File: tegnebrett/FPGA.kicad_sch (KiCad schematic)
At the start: 28 parts, among them J6 FPGA_debug1, J7 FPGA_Header_Pin, SW6 FPGA_Button, U2 XC7A100T-2FTG256I, U3 Oscillator 100MHz, U4 IS66WVH16M8DBLL-100B1LI1

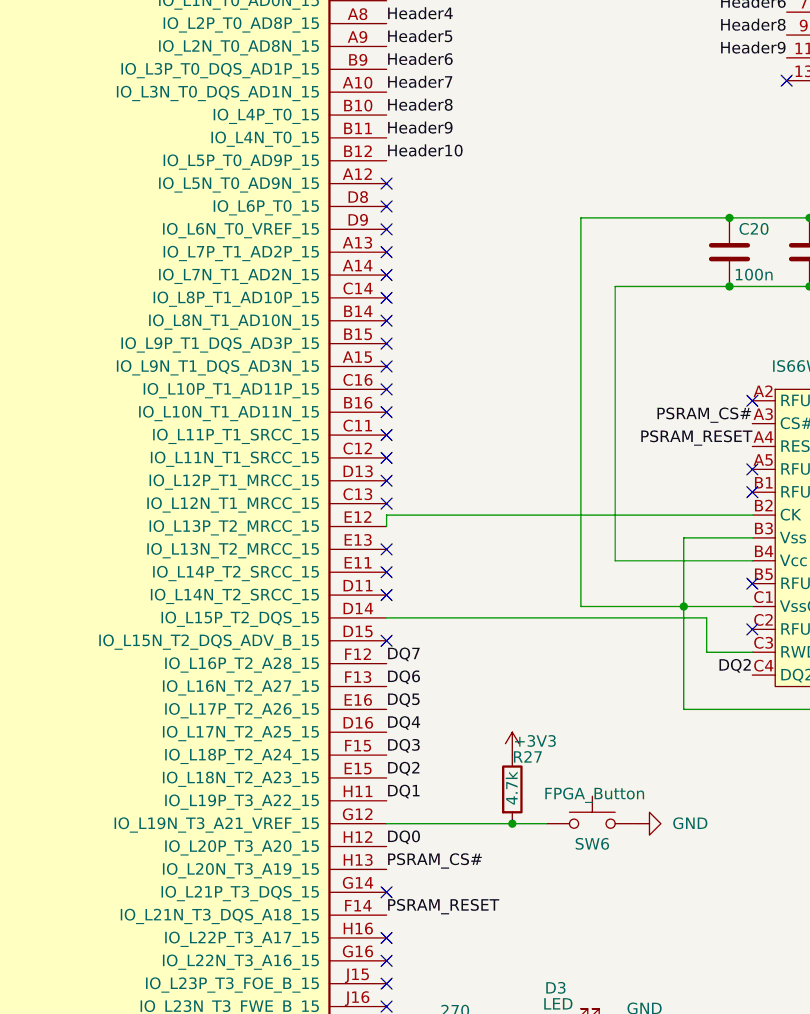
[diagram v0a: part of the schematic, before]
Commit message: refactor(FPGA): move DQ0 pin to reference to different GPIO pin
As Tormod wrote on Discord:
H12 (DQ0) -> A12 (IO_L5N_TO_AD9N_15)
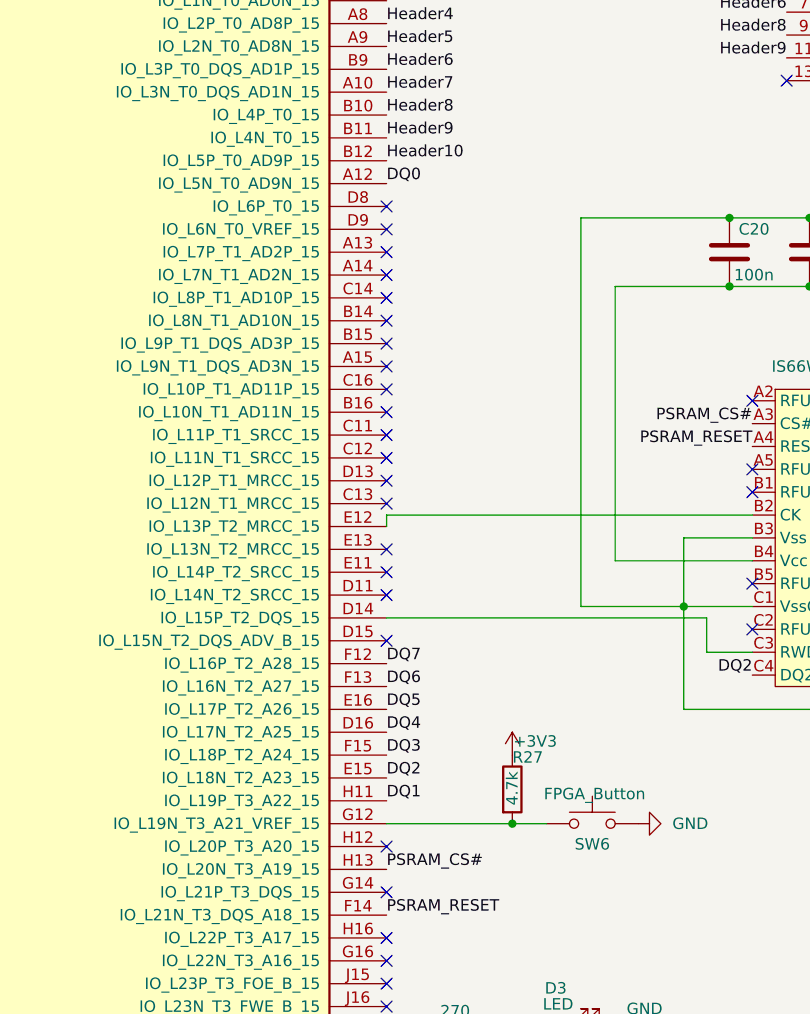
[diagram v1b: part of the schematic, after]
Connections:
- net DQ0: now also U2.A12 (IO_L5N_T0_AD9N_15); no longer U2.H12 (IO_L20P_T3_A20_15)
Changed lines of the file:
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@@
+	)
+	(no_connect
+		(at 320.04 147.32)
 	)
 	(no_connect
@@
 	(no_connect
 		(at 360.68 97.79)
-	)
-	(no_connect
-		(at 320.04 73.66)
 	)
 	(no_connect
@@
 		)
 	)
-	(label "DQ0"
-		(at 320.04 147.32 0)
-		(effects
-			(font
-				(size 1.27 1.27)
-			)
-			(justify left bottom)
-		)
-	)
 	(label "DQ5"
 		(at 391.16 119.38 0)
@@
 		(effects
 			(font
+				(size 1.27 1.27)
+			)
+			(justify left bottom)
+		)
+	)
+	(label "DQ0"
+		(at 320.04 73.66 0)
+		(effects
+			(font

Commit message: fix: add FPGA debug symbol to tegnebrett_symbols library
This was a symbol added by Tormod which has also been lost to time.
No problems, we just save the symbol into *tegnebrett_symbols*.

I believe we will change the pin functions as well.
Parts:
- J6: value FPGA_debug1 -> FPGA_debug; symbol GD25F128FS2GR:FPGA_debug -> tegnebrett_symbols:FPGA_debug
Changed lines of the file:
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@@
 	)
 	(symbol
-		(lib_id "GD25F128FS2GR:FPGA_debug")
+		(lib_id "tegnebrett_symbols:FPGA_debug")
 		(at 106.68 21.59 0)
 		(mirror y)
@@
 			)
 		)
-		(property "Value" "FPGA_debug1"
+		(property "Value" "FPGA_debug"
 			(at 107.95 20.32 0)
 			(effects

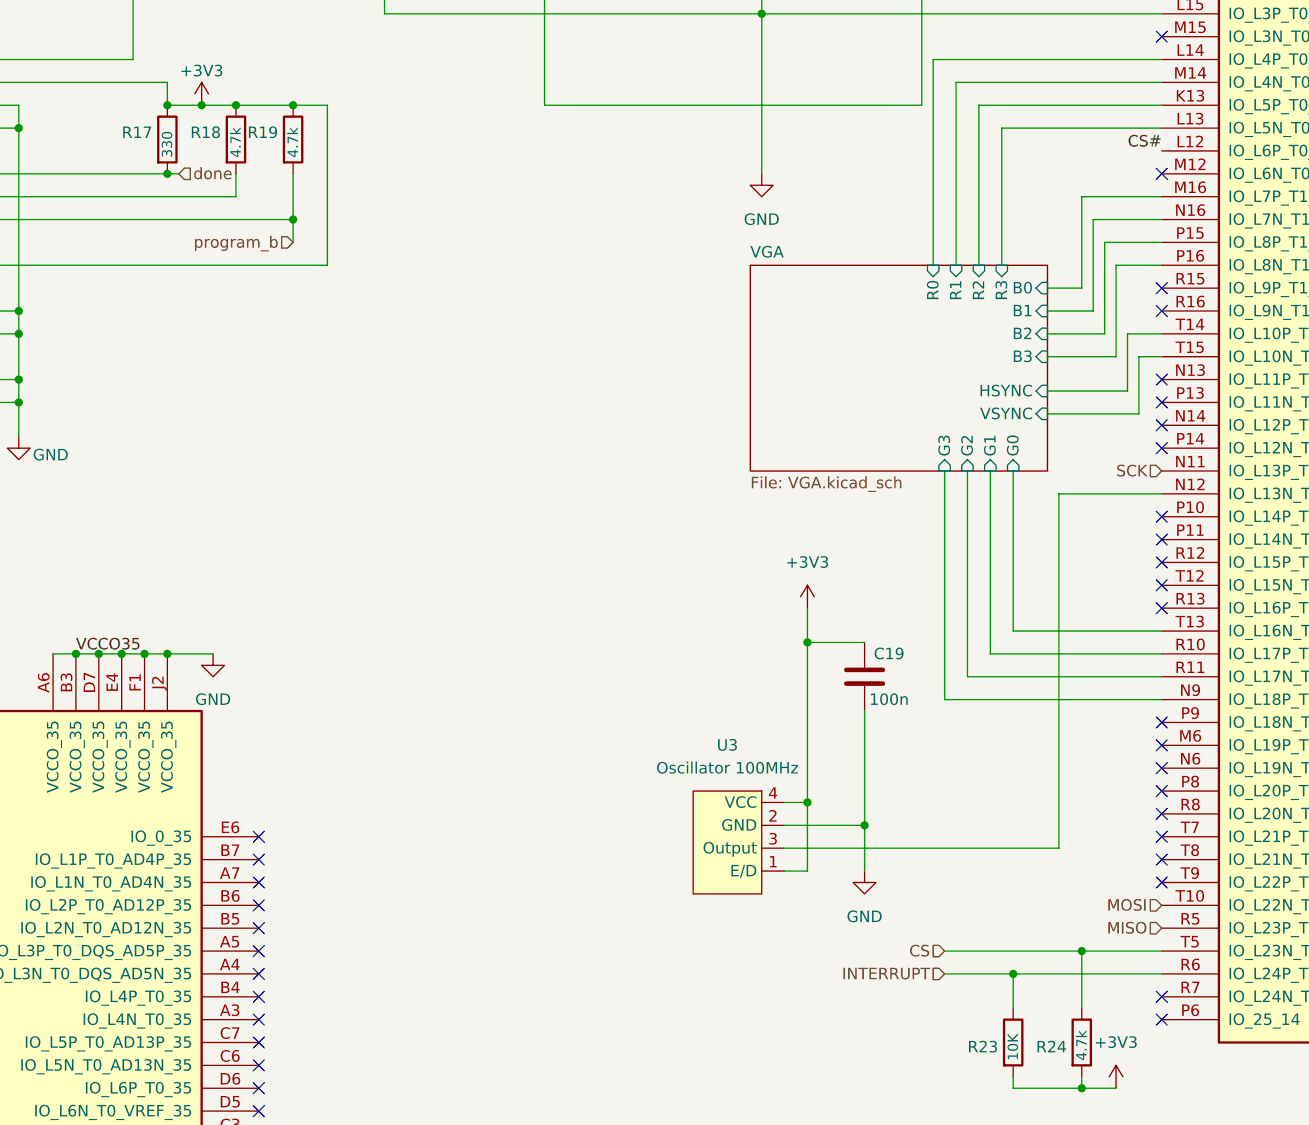
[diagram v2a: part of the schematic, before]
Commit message: refactor: Update label names for hierarchical labels.
Renamed the hierarchical labels in FPGA.kicad_sch, they now are named
the say as the local labels in tegnebrett.kicad_sch

This results in KiCAD no longer throwing any warnings telling us that we
have labels which only differ in casing (upper case / lower case).
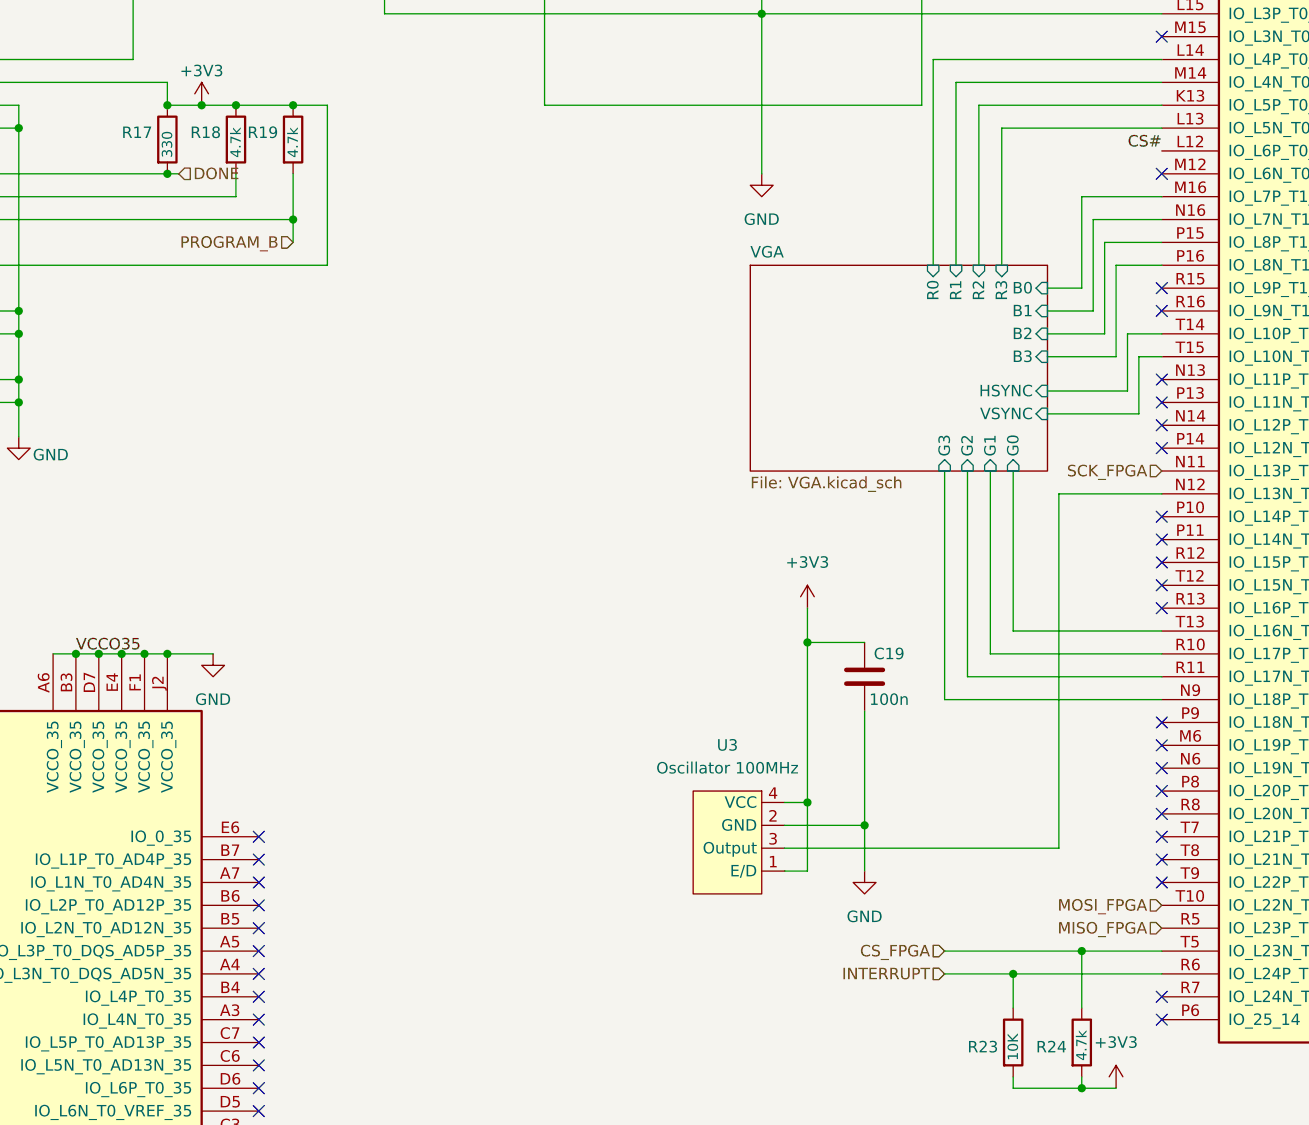
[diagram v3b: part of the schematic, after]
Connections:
- net CS renamed CS_FPGA
- net MISO renamed MISO_FPGA
- net MOSI renamed MOSI_FPGA
- net SCK renamed SCK_FPGA
- net done renamed DONE
- net program_b renamed PROGRAM_B
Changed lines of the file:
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@@
 		)
 	)
-	(hierarchical_label "MISO"
+	(hierarchical_label "MISO_FPGA"
 		(shape input)
 		(at 218.44 162.56 180)
@@
 		)
 	)
-	(hierarchical_label "done"
+	(hierarchical_label "DONE"
 		(shape input)
 		(at 109.22 78.74 0)
@@
 		)
 	)
-	(hierarchical_label "SCK"
+	(hierarchical_label "SCK_FPGA"
 		(shape input)
 		(at 218.44 111.76 180)
@@
 		)
 	)
-	(hierarchical_label "program_b"
+	(hierarchical_label "PROGRAM_B"
 		(shape input)
 		(at 121.92 86.36 180)
@@
 		)
 	)
-	(hierarchical_label "MOSI"
+	(hierarchical_label "MOSI_FPGA"
 		(shape input)
 		(at 218.44 160.02 180)
@@
 		)
 	)
-	(hierarchical_label "CS"
+	(hierarchical_label "CS_FPGA"
 		(shape input)
 		(at 194.31 165.1 180)

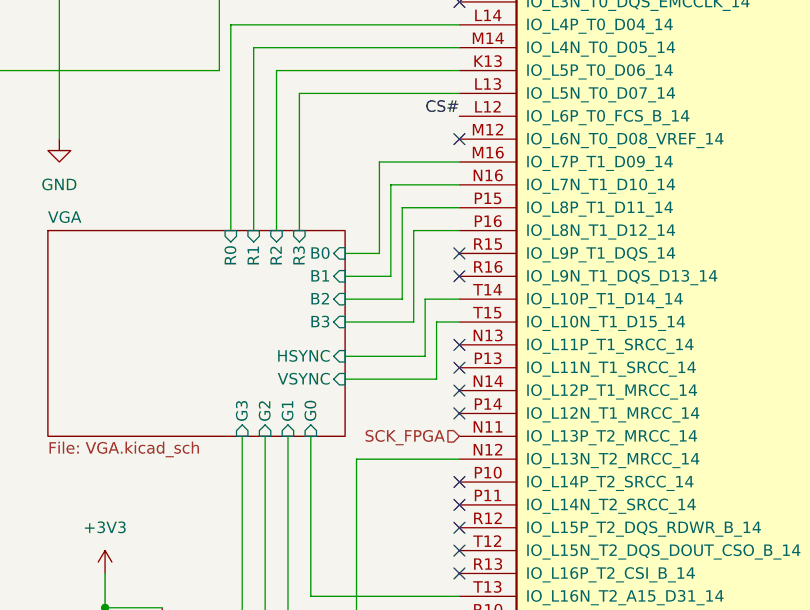
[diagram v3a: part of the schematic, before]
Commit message: refactor: move SCK_FPGA from N11 to N14
This allows for easier routing on the PCB.
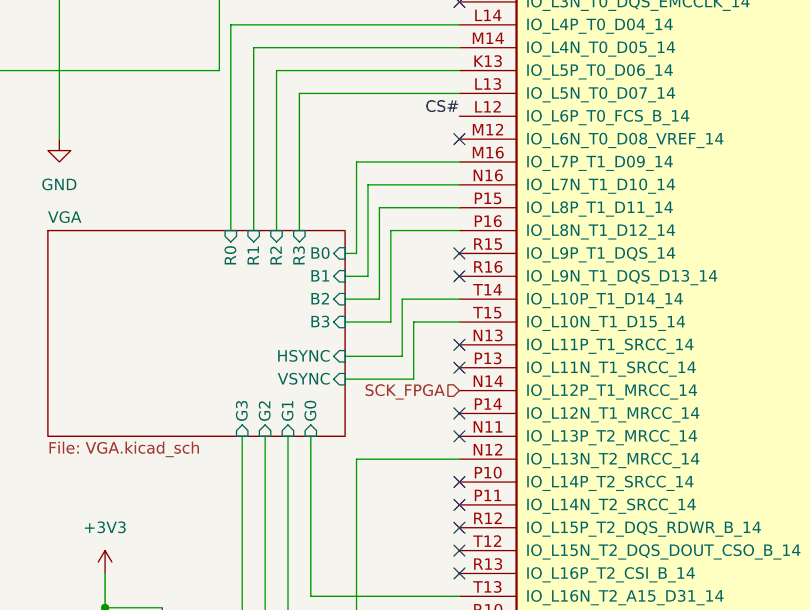
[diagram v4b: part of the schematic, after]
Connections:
- net SCK_FPGA: now also U2.N14 (IO_L12P_T1_MRCC_14); no longer U2.N11 (IO_L13P_T2_MRCC_14)
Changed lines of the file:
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@@
-	)
-	(no_connect
-		(at 218.44 106.68)
 	)
 	(no_connect
@@
 	)
 	(no_connect
+		(at 218.44 101.6)
+	)
+	(no_connect
 		(at 118.11 276.86)
 	)
@@
 	)
 	(no_connect
-		(at 218.44 101.6)
-	)
-	(no_connect
 		(at 118.11 226.06)
 	)
@@
 		(at 218.44 104.14)
 	)
+	(no_connect
+		(at 218.44 111.76)
+	)
 	(wire
 		(pts
@@
 	(wire
 		(pts
-			(xy 214.63 96.52) (xy 214.63 102.87)
+			(xy 212.09 96.52) (xy 212.09 102.87)
 		)
 		(stroke
@@
 	(wire
 		(pts
-			(xy 215.9 105.41) (xy 215.9 99.06)
-		)
-		(stroke
-			(width 0)
-			(type default)
-		)
-	)
-	(wire
-		(pts
 			(xy 201.93 167.64) (xy 218.44 167.64)
 		)
@@
 	(wire
 		(pts
-			(xy 205.74 105.41) (xy 215.9 105.41)
-		)
-		(stroke
-			(width 0)
-			(type default)
-		)
-	)
-	(wire
-		(pts
 			(xy 367.03 77.47) (xy 374.65 77.47)
 		)
@@
 	(wire
 		(pts
-			(xy 210.82 93.98) (xy 205.74 93.98)
+			(xy 208.28 93.98) (xy 205.74 93.98)
 		)
 		(stroke
@@
 	(wire
 		(pts
-			(xy 209.55 81.28) (xy 218.44 81.28)
-		)
-		(stroke
-			(width 0)
-			(type default)
-		)
-	)
-	(wire
-		(pts
-			(xy 213.36 99.06) (xy 205.74 99.06)
+			(xy 207.01 81.28) (xy 218.44 81.28)
 		)
 		(stroke
@@
 	(wire
 		(pts
-			(xy 205.74 96.52) (xy 212.09 96.52)
+			(xy 205.74 99.06) (xy 210.82 99.06)
 		)
 		(stroke
@@
 	(wire
 		(pts
+			(xy 205.74 102.87) (xy 212.09 102.87)
+		)
+		(stroke
+			(width 0)
+			(type default)
+		)
+	)
+	(wire
+		(pts
 			(xy 114.3 31.75) (xy 114.3 34.29)
 		)
@@
 	(wire
 		(pts
+			(xy 213.36 105.41) (xy 213.36 99.06)
+		)
+		(stroke
+			(width 0)
+			(type default)
+		)
+	)
+	(wire
+		(pts
 			(xy 358.14 77.47) (xy 341.63 77.47)
 		)
@@
 	(wire
 		(pts
-			(xy 218.44 83.82) (xy 210.82 83.82)
+			(xy 218.44 83.82) (xy 208.28 83.82)
 		)
 		(stroke
@@
 	(wire
 		(pts
+			(xy 205.74 96.52) (xy 209.55 96.52)
+		)
+		(stroke
+			(width 0)
+			(type default)
+		)
+	)
+	(wire
+		(pts
 			(xy 194.31 137.16) (xy 194.31 111.76)
 		)
@@
 	(wire
 		(pts
-			(xy 214.63 102.87) (xy 205.74 102.87)
-		)
-		(stroke
-			(width 0)
-			(type default)
-		)
-	)
-	(wire
-		(pts
 			(xy 209.55 180.34) (xy 201.93 180.34)
 		)
@@
 	(wire
 		(pts
-			(xy 218.44 96.52) (xy 214.63 96.52)
+			(xy 218.44 96.52) (xy 212.09 96.52)
 		)
 		(stroke
@@
 	(wire
 		(pts
-			(xy 218.44 88.9) (xy 213.36 88.9)
+			(xy 218.44 88.9) (xy 210.82 88.9)
 		)
 		(stroke
@@
 	(wire
 		(pts
-			(xy 213.36 88.9) (xy 213.36 99.06)
+			(xy 210.82 88.9) (xy 210.82 99.06)
 		)
 		(stroke
@@
 	(wire
 		(pts
-			(xy 212.09 96.52) (xy 212.09 86.36)
-		)
-		(stroke
-			(width 0)
-			(type default)
-		)
-	)
-	(wire
-		(pts
 			(xy 132.08 34.29) (xy 144.78 34.29)
 		)
@@
 	(wire
 		(pts
-			(xy 210.82 83.82) (xy 210.82 93.98)
+			(xy 208.28 83.82) (xy 208.28 93.98)
 		)
 		(stroke
@@
 	(wire
 		(pts
-			(xy 205.74 91.44) (xy 209.55 91.44)
+			(xy 205.74 91.44) (xy 207.01 91.44)
 		)
 		(stroke
@@
 	(wire
 		(pts
+			(xy 209.55 96.52) (xy 209.55 86.36)
+		)
+		(stroke
+			(width 0)
+			(type default)
+		)
+	)
+	(wire
+		(pts
 			(xy 121.92 83.82) (xy 121.92 78.74)
 		)
@@
 	(wire
 		(pts
-			(xy 209.55 91.44) (xy 209.55 81.28)
+			(xy 207.01 91.44) (xy 207.01 81.28)
 		)
 		(stroke
@@
 	(wire
 		(pts
-			(xy 215.9 99.06) (xy 218.44 99.06)
-		)
-		(stroke
-			(width 0)
-			(type default)
-		)
-	)
-	(wire
-		(pts
-			(xy 212.09 86.36) (xy 218.44 86.36)
+			(xy 213.36 99.06) (xy 218.44 99.06)
+		)
+		(stroke
+			(width 0)
+			(type default)
+		)
+	)
+	(wire
+		(pts
+			(xy 209.55 86.36) (xy 218.44 86.36)
 		)
 		(stroke
@@
 		(pts
 			(xy 218.44 50.8) (xy 191.77 50.8)
+		)
+		(stroke
+			(width 0)
+			(type default)
+		)
+	)
+	(wire
+		(pts
+			(xy 205.74 105.41) (xy 213.36 105.41)
 		)
 		(stroke
@@
 	(hierarchical_label "SCK_FPGA"
 		(shape input)
-		(at 218.44 111.76 180)
-		(effects
-			(font
+		(at 218.44 106.68 180)
+		(effects
+			(font

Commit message: fix: add FPGA Oscillator 100MHz to tegnebrett_symbols file
This is one symbol which Tormod created locally which got lost to time.
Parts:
- U3: symbol XC7A100T-2FTG256I:CWX813-100.0M -> tegnebrett_symbols:CWX813-100.0M
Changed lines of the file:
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@@
 	)
 	(symbol
-		(lib_id "XC7A100T-2FTG256I:CWX813-100.0M")
+		(lib_id "tegnebrett_symbols:CWX813-100.0M")
 		(at 173.99 144.78 0)
 		(mirror y)

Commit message: fix: add FPGA Flash to tegnebrett_symbols.kicad_sch
Once again, a symbol which has got lost to time.
This removes yet another warning when doing the ERC check.
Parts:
- F1: symbol GD25F128FS2GR:GD25F128FS2GR -> tegnebrett_symbols:GD25F128FS2GR
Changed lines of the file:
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@@
 	)
 	(symbol
-		(lib_id "GD25F128FS2GR:GD25F128FS2GR")
+		(lib_id "tegnebrett_symbols:GD25F128FS2GR")
 		(at 161.29 44.45 0)
 		(mirror y)
